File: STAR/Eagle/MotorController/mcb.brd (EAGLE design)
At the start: 28 x 35.5 mm, 38 parts, among them J1 J30J-9J30, U1 ATMEGA328P-MU, U2 A4988SETTR-T, U3 LT3010, U4 LT8630

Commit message: mcb update
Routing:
- net GND: track 192.5 -> 192.6 mm, vias 23 -> 25
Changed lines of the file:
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@@
 <setting verticaltext="up"/>
 </settings>
-<grid distance="0.1" unitdist="mm" unit="mm" style="lines" multiple="1" display="yes" altdistance="0.025" altunitdist="inch" altunit="inch"/>
+<grid distance="0.05" unitdist="mm" unit="mm" style="lines" multiple="1" display="yes" altdistance="0.025" altunitdist="inch" altunit="inch"/>
 <layers>
 <layer number="1" name="Top" color="4" fill="1" visible="yes" active="yes"/>
@@
 <wire x1="8.51" y1="10.2" x2="7.6" y2="10.2" width="0.3048" layer="1"/>
 <via x="7.6" y="10.2" extent="1-16" drill="0.5"/>
-<wire x1="7.6" y1="10.2" x2="6.1" y2="8.7" width="0.3048" layer="16"/>
-<via x="6.1" y="8.7" extent="1-16" drill="0.5"/>
-<wire x1="6.1" y1="8.7" x2="5.87" y2="8.47" width="0.3048" layer="1"/>
+<wire x1="7.6" y1="10.2" x2="6" y2="8.9" width="0.3048" layer="16"/>
+<via x="6" y="8.9" extent="1-16" drill="0.5"/>
+<wire x1="6" y1="8.9" x2="5.87" y2="8.47" width="0.3048" layer="1"/>
 <wire x1="5.87" y1="8.47" x2="5.19" y2="8.47" width="0.3048" layer="1"/>
 <wire x1="13.97" y1="17.41" x2="14.1" y2="17.54" width="0.254" layer="1"/>
@@
 <wire x1="22.7" y1="0.6" x2="22.7" y2="1.3" width="0.3048" layer="1"/>
 <via x="21.1" y="17.6" extent="1-16" drill="0.5"/>
+<via x="6.7" y="33.05" extent="1-16" drill="0.5"/>
+<via x="9.4" y="24.4" extent="1-16" drill="0.5"/>
 </signal>
 <signal name="+5V">
@@
 <wire x1="17.25" y1="17" x2="15.5" y2="17" width="0.3048" layer="16"/>
 <wire x1="15.5" y1="17" x2="14.5" y2="16" width="0.3048" layer="16"/>
-<wire x1="14.5" y1="16" x2="14.5" y2="15" width="0.3048" layer="16"/>
-<via x="14.5" y="15" extent="1-16" drill="0.5"/>
+<wire x1="14.5" y1="16" x2="14.5" y2="14.8" width="0.3048" layer="16"/>
+<via x="14.5" y="14.8" extent="1-16" drill="0.5"/>
 <wire x1="16.352" y1="12.3822" x2="16.352" y2="12.898" width="0.3048" layer="1"/>
 <wire x1="16.352" y1="12.898" x2="15.25" y2="14" width="0.3048" layer="1"/>
 <wire x1="15.25" y1="14" x2="15.25" y2="14.5" width="0.3048" layer="1"/>
-<wire x1="15.25" y1="14.5" x2="14.75" y2="15" width="0.3048" layer="1"/>
-<wire x1="14.75" y1="15" x2="14.5" y2="15" width="0.3048" layer="1"/>
+<wire x1="15.25" y1="14.5" x2="14.95" y2="14.8" width="0.3048" layer="1"/>
+<wire x1="14.95" y1="14.8" x2="14.5" y2="14.8" width="0.3048" layer="1"/>
 </signal>
 <signal name="STEP">
@@
 <wire x1="21.7794" y1="9.0294" x2="22.25" y2="9.5" width="0.3048" layer="1"/>
 <via x="22.25" y="9.5" extent="1-16" drill="0.5"/>
-<wire x1="22.25" y1="9.5" x2="22.25" y2="10.5" width="0.3048" layer="16"/>
-<wire x1="22.25" y1="10.5" x2="17" y2="15.75" width="0.3048" layer="16"/>
 <via x="17" y="15.75" extent="1-16" drill="0.5"/>
 <wire x1="17.948" y1="16.698" x2="18.6562" y2="16.698" width="0.3048" layer="1"/>
 <wire x1="17" y1="15.75" x2="17.948" y2="16.698" width="0.3048" layer="1"/>
+<wire x1="17" y1="15.75" x2="17" y2="15.65" width="0.3048" layer="16"/>
+<wire x1="17" y1="15.65" x2="19.2" y2="13.45" width="0.3048" layer="16"/>
+<wire x1="19.2" y1="13.45" x2="19.3" y2="13.35" width="0.3048" layer="16"/>
+<wire x1="22.25" y1="9.5" x2="22.25" y2="10.4" width="0.3048" layer="16"/>
+<wire x1="22.25" y1="10.4" x2="19.3" y2="13.35" width="0.3048" layer="16"/>
 </signal>
 <signal name="MS2">
@@
 <wire x1="20.238" y1="9.512" x2="20.15" y2="9.5" width="0.3048" layer="1"/>
 <via x="20.15" y="9.5" extent="1-16" drill="0.5"/>
-<via x="16.25" y="14.75" extent="1-16" drill="0.5"/>
+<via x="16.45" y="14.75" extent="1-16" drill="0.5"/>
 <wire x1="18.2154" y1="16.2154" x2="18.6562" y2="16.2154" width="0.3048" layer="1"/>
 <wire x1="20.25" y1="10.5" x2="17" y2="13.75" width="0.3048" layer="16"/>
 <wire x1="17" y1="13.75" x2="17" y2="14.25" width="0.3048" layer="16"/>
-<wire x1="17" y1="14.25" x2="16.5" y2="14.75" width="0.3048" layer="16"/>
-<wire x1="16.5" y1="14.75" x2="16.25" y2="14.75" width="0.3048" layer="16"/>
-<wire x1="16.25" y1="14.75" x2="17" y2="14.75" width="0.3048" layer="1"/>
 <wire x1="17" y1="14.75" x2="17.75" y2="15.5" width="0.3048" layer="1"/>
 <wire x1="18.2154" y1="16.2154" x2="17.75" y2="15.75" width="0.3048" layer="1"/>
@@
 <wire x1="19.2222" y1="9.512" x2="20.138" y2="9.512" width="0.3048" layer="1"/>
 <wire x1="20.138" y1="9.512" x2="20.15" y2="9.5" width="0.3048" layer="1"/>
+<wire x1="17" y1="14.25" x2="16.5" y2="14.75" width="0.3048" layer="16"/>
+<wire x1="16.5" y1="14.75" x2="16.45" y2="14.75" width="0.3048" layer="16"/>
+<wire x1="17" y1="14.75" x2="16.45" y2="14.75" width="0.3048" layer="1"/>
 </signal>
 <signal name="MS3">
@@
 <via x="21.25" y="10" extent="1-16" drill="0.5"/>
 <wire x1="21.25" y1="10" x2="21.25" y2="10.25" width="0.3048" layer="16"/>
-<wire x1="21.25" y1="10.25" x2="17.5" y2="14" width="0.3048" layer="16"/>
-<via x="17.5" y="14" extent="1-16" drill="0.5"/>
-<wire x1="17.5" y1="14" x2="17.5" y2="14.5512" width="0.3048" layer="1"/>
-<wire x1="17.5" y1="14.5512" x2="18.6562" y2="15.7074" width="0.3048" layer="1"/>
+<via x="17.7" y="14.1" extent="1-16" drill="0.5"/>
+<wire x1="21.25" y1="10.25" x2="17.7" y2="13.8" width="0.3048" layer="16"/>
+<wire x1="17.7" y1="13.8" x2="17.7" y2="14.1" width="0.3048" layer="16"/>
+<wire x1="17.7" y1="14.1" x2="17.7" y2="14.7512" width="0.3048" layer="1"/>
+<wire x1="17.7" y1="14.7512" x2="18.6562" y2="15.7074" width="0.3048" layer="1"/>
 </signal>
 <signal name="RESET~">

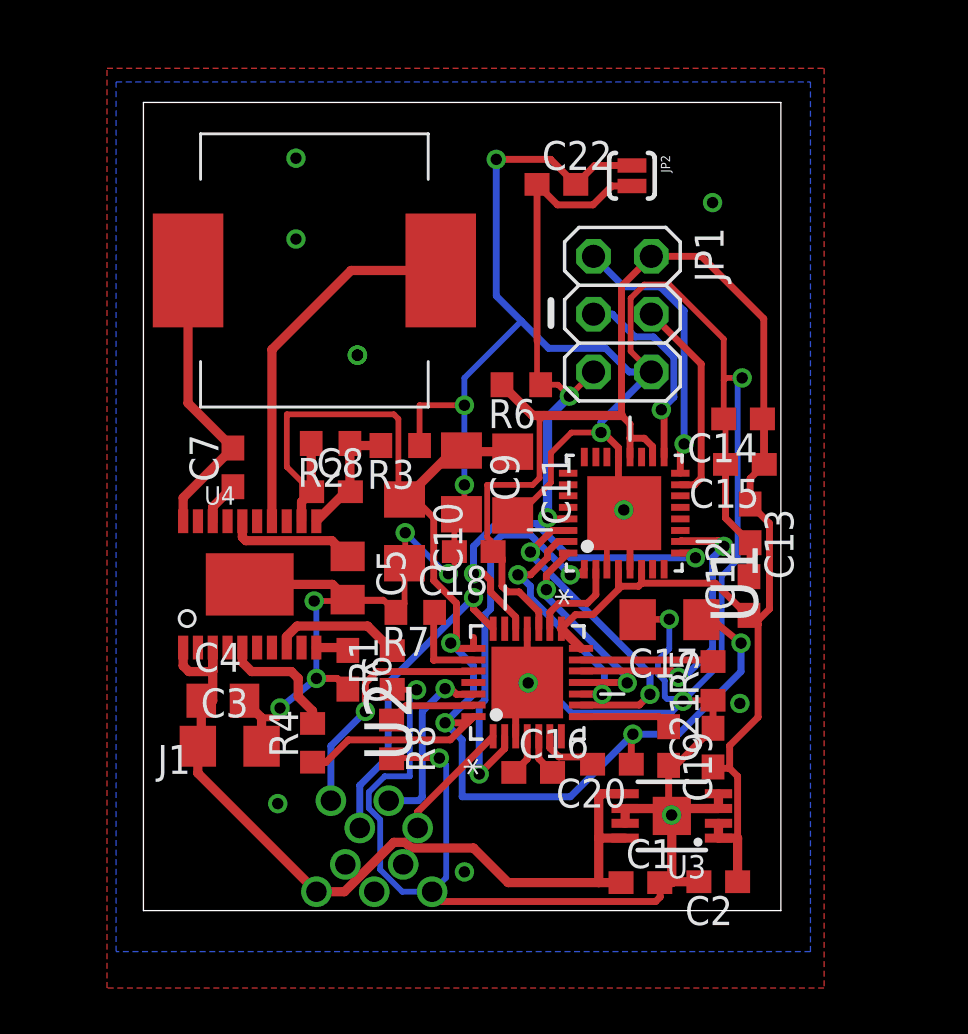
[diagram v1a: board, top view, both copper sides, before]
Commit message: increased room for C16
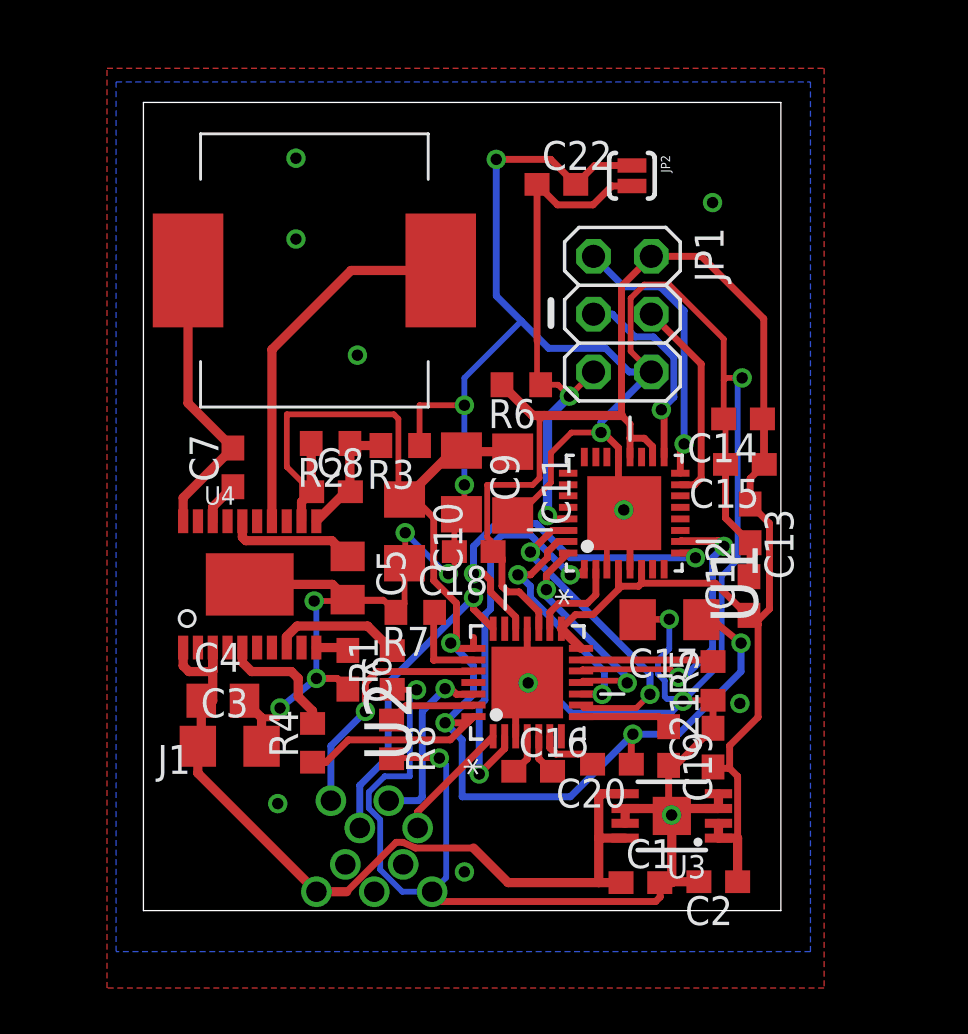
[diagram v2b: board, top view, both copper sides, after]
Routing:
- net GND: vias 25 -> 24
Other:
- board text added: "UMDBPP ROCKSAT-X 2018 MCB Rev 1.0"
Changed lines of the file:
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@@
 <setting verticaltext="up"/>
 </settings>
-<grid distance="0.05" unitdist="mm" unit="mm" style="lines" multiple="1" display="yes" altdistance="0.025" altunitdist="inch" altunit="inch"/>
+<grid distance="0.1" unitdist="mm" unit="mm" style="lines" multiple="1" display="yes" altdistance="0.025" altunitdist="inch" altunit="inch"/>
 <layers>
 <layer number="1" name="Top" color="4" fill="1" visible="yes" active="yes"/>
@@
 <layer number="20" name="Dimension" color="15" fill="1" visible="yes" active="yes"/>
 <layer number="21" name="tPlace" color="7" fill="1" visible="yes" active="yes"/>
-<layer number="22" name="bPlace" color="7" fill="1" visible="no" active="yes"/>
-<layer number="23" name="tOrigins" color="15" fill="1" visible="yes" active="yes"/>
+<layer number="22" name="bPlace" color="7" fill="1" visible="yes" active="yes"/>
+<layer number="23" name="tOrigins" color="15" fill="1" visible="no" active="yes"/>
 <layer number="24" name="bOrigins" color="15" fill="1" visible="no" active="yes"/>
 <layer number="25" name="tNames" color="7" fill="1" visible="no" active="yes"/>
@@
 <dimension x1="0" y1="0" x2="28" y2="0" x3="14" y3="-4.8" textsize="1.778" layer="51"/>
 <dimension x1="28" y1="35.5" x2="28" y2="0" x3="36.7" y3="17.75" textsize="1.778" layer="51"/>
+<text x="4.9" y="11.1" size="1.016" layer="22" rot="MR270">UMDBPP
+ROCKSAT-X 2018
+MCB Rev 1.0</text>
 </plain>
 <attributes>
@@
 <element name="C14" library="resistor" package="C0603" value="1uF" x="26.34" y="21.6" rot="R180"/>
 <element name="C15" library="resistor" package="C0603" value="1uF" x="26.42" y="19.6" rot="R180"/>
-<element name="C16" library="resistor" package="C0603" value="100nF" x="17.12" y="6.07"/>
+<element name="C16" library="resistor" package="C0603" value="100nF" x="17.12" y="6.12"/>
 <element name="C17" library="resistor" package="C1206" value="10uF" x="23.11" y="12.78" rot="R180"/>
 <element name="C18" library="resistor" package="C0603" value="1uF" x="14.51" y="15.77" rot="R180"/>
@@
 </polygon>
 <via x="6.7" y="29.5" extent="1-16" drill="0.5"/>
-<via x="9.4" y="24.4" extent="1-16" drill="0.5"/>
 <via x="25" y="31.1" extent="1-16" drill="0.5"/>
 <via x="26.2" y="9.1" extent="1-16" drill="0.5"/>
@@
 <wire x1="7.6" y1="0.83" x2="2.39" y2="6.04" width="0.4064" layer="1"/>
 <wire x1="2.39" y1="6.04" x2="2.39" y2="7.22" width="0.4064" layer="1"/>
-<wire x1="7.6" y1="0.83" x2="8.83" y2="0.83" width="0.4064" layer="1"/>
-<wire x1="8.83" y1="0.83" x2="11" y2="3" width="0.4064" layer="1"/>
-<wire x1="11" y1="3" x2="11.5" y2="3" width="0.4064" layer="1"/>
-<wire x1="11.5" y1="3" x2="11.75" y2="2.75" width="0.4064" layer="1"/>
-<wire x1="11.75" y1="2.75" x2="14.5" y2="2.75" width="0.4064" layer="1"/>
+<wire x1="7.6" y1="0.83" x2="8.93" y2="0.83" width="0.4064" layer="1"/>
+<wire x1="8.93" y1="0.83" x2="11.1" y2="3" width="0.3048" layer="1"/>
+<wire x1="11.1" y1="3" x2="11.4" y2="3" width="0.3048" layer="1"/>
+<wire x1="11.4" y1="3" x2="11.95" y2="2.75" width="0.3048" layer="1"/>
+<wire x1="11.95" y1="2.75" x2="14.5" y2="2.75" width="0.3048" layer="1"/>
 <wire x1="14.5" y1="2.75" x2="16.02" y2="1.23" width="0.4064" layer="1"/>
 <wire x1="16.02" y1="1.23" x2="20" y2="1.23" width="0.4064" layer="1"/>
@@
 <contactref element="U2" pad="5"/>
 <contactref element="C16" pad="2"/>
-<wire x1="17.97" y1="6.07" x2="17.368" y2="6.672" width="0.3048" layer="1"/>
+<wire x1="17.97" y1="6.12" x2="17.368" y2="6.672" width="0.3048" layer="1"/>
 <wire x1="17.368" y1="6.672" x2="17.368" y2="7.6578" width="0.3048" layer="1"/>
 </signal>
@@
 <contactref element="C16" pad="1"/>
 <contactref element="U2" pad="4"/>
-<wire x1="16.27" y1="6.07" x2="16.86" y2="6.66" width="0.3048" layer="1"/>
+<wire x1="16.27" y1="6.12" x2="16.86" y2="6.66" width="0.3048" layer="1"/>
 <wire x1="16.86" y1="6.66" x2="16.86" y2="7.6578" width="0.3048" layer="1"/>
 </signal>
@@
 <contactref element="C20" pad="2"/>
 <wire x1="17.8506" y1="7.6578" x2="17.8506" y2="7.1494" width="0.3048" layer="1"/>
-<wire x1="17.8506" y1="7.1494" x2="18.25" y2="6.75" width="0.3048" layer="1"/>
-<wire x1="18.25" y1="6.75" x2="19.41" y2="6.75" width="0.3048" layer="1"/>
-<wire x1="19.41" y1="6.75" x2="19.73" y2="6.43" width="0.3048" layer="1"/>
+<wire x1="17.8506" y1="7.1494" x2="18.125" y2="6.875" width="0.3048" layer="1"/>
+<wire x1="18.125" y1="6.875" x2="19.285" y2="6.875" width="0.3048" layer="1"/>
+<wire x1="19.285" y1="6.875" x2="19.73" y2="6.43" width="0.3048" layer="1"/>
 </signal>
 <signal name="ENABLE~">
@@
 <contactref element="U2" pad="9"/>
 <contactref element="U1" pad="30"/>
-<wire x1="19.2222" y1="9.0294" x2="21.7794" y2="9.0294" width="0.3048" layer="1"/>
-<wire x1="21.7794" y1="9.0294" x2="22.25" y2="9.5" width="0.3048" layer="1"/>
 <via x="22.25" y="9.5" extent="1-16" drill="0.5"/>
 <via x="17" y="15.75" extent="1-16" drill="0.5"/>
@@
 <wire x1="17" y1="15.75" x2="17.948" y2="16.698" width="0.3048" layer="1"/>
 <wire x1="17" y1="15.75" x2="17" y2="15.65" width="0.3048" layer="16"/>
-<wire x1="17" y1="15.65" x2="19.2" y2="13.45" width="0.3048" layer="16"/>
-<wire x1="19.2" y1="13.45" x2="19.3" y2="13.35" width="0.3048" layer="16"/>
 <wire x1="22.25" y1="9.5" x2="22.25" y2="10.4" width="0.3048" layer="16"/>
-<wire x1="22.25" y1="10.4" x2="19.3" y2="13.35" width="0.3048" layer="16"/>
+<wire x1="22.25" y1="10.4" x2="17" y2="15.65" width="0.3048" layer="16"/>
+<wire x1="19.2222" y1="9.0294" x2="19.3516" y2="8.9" width="0.254" layer="1"/>
+<wire x1="19.3516" y1="8.9" x2="21.65" y2="8.9" width="0.254" layer="1"/>
+<wire x1="21.65" y1="8.9" x2="22.25" y2="9.5" width="0.254" layer="1"/>
 </signal>
 <signal name="MS2">
@@
 <contactref element="U2" pad="11"/>
 <contactref element="U1" pad="32"/>
-<wire x1="19.2222" y1="10.02" x2="21.23" y2="10.02" width="0.3048" layer="1"/>
 <wire x1="21.23" y1="10.02" x2="21.25" y2="10" width="0.3048" layer="1"/>
 <via x="21.25" y="10" extent="1-16" drill="0.5"/>
@@
 <wire x1="17.7" y1="14.1" x2="17.7" y2="14.7512" width="0.3048" layer="1"/>
 <wire x1="17.7" y1="14.7512" x2="18.6562" y2="15.7074" width="0.3048" layer="1"/>
+<wire x1="19.2222" y1="10.02" x2="19.3022" y2="10.1" width="0.254" layer="1"/>
+<wire x1="19.3022" y1="10.1" x2="21.15" y2="10.1" width="0.254" layer="1"/>
+<wire x1="21.15" y1="10.1" x2="21.25" y2="10" width="0.254" layer="1"/>
 </signal>
 <signal name="RESET~">
 <contactref element="U2" pad="12"/>
 <contactref element="U1" pad="10"/>
-<wire x1="19.2222" y1="10.528" x2="23.222" y2="10.528" width="0.3048" layer="1"/>
-<wire x1="23.222" y1="10.528" x2="23.5" y2="10.25" width="0.3048" layer="1"/>
 <via x="23.5" y="10.25" extent="1-16" drill="0.5"/>
 <wire x1="25.5" y1="16" x2="25.2846" y2="16.2154" width="0.3048" layer="1"/>
@@
 <wire x1="25" y1="11.5" x2="23.75" y2="10.25" width="0.3048" layer="16"/>
 <wire x1="23.75" y1="10.25" x2="23.5" y2="10.25" width="0.3048" layer="16"/>
+<wire x1="19.2222" y1="10.528" x2="19.2942" y2="10.6" width="0.254" layer="1"/>
+<wire x1="19.2942" y1="10.6" x2="23.15" y2="10.6" width="0.254" layer="1"/>
+<wire x1="23.15" y1="10.6" x2="23.5" y2="10.25" width="0.254" layer="1"/>
 </signal>
 <signal name="MOSI">
@@
 <via x="18.71" y="22.6" extent="1-16" drill="0.5"/>
 <wire x1="18.71" y1="22.6" x2="17.75" y2="21.64" width="0.4064" layer="16"/>
-<wire x1="17.75" y1="21.64" x2="17.75" y2="17.25" width="0.4064" layer="16"/>
-<via x="17.75" y="17.25" extent="1-16" drill="0.5"/>
-<wire x1="17.75" y1="17.25" x2="17.794" y2="17.206" width="0.3048" layer="1"/>
-<wire x1="17.794" y1="17.206" x2="18.6562" y2="17.206" width="0.3048" layer="1"/>
+<wire x1="17.75" y1="21.64" x2="17.75" y2="17.35" width="0.4064" layer="16"/>
+<via x="17.75" y="17.35" extent="1-16" drill="0.5"/>
+<wire x1="17.75" y1="17.35" x2="17.894" y2="17.206" width="0.3048" layer="1"/>
+<wire x1="17.894" y1="17.206" x2="18.6562" y2="17.206" width="0.3048" layer="1"/>
 <wire x1="18.71" y1="22.6" x2="19.77" y2="23.66" width="0.254" layer="1"/>
 <wire x1="18.71" y1="22.6" x2="18.21" y2="23.1" width="0.254" layer="1"/>
@@
 </board>
 </drawing>
+<compatibility>
+<note version="6.3" minversion="6.2.2" severity="warning">
+Since Version 6.2.2 text objects can contain more than one line,
+which will not be processed correctly with this version.
+</note>
+</compatibility>
 </eagle>

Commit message: mounting holes on mcb
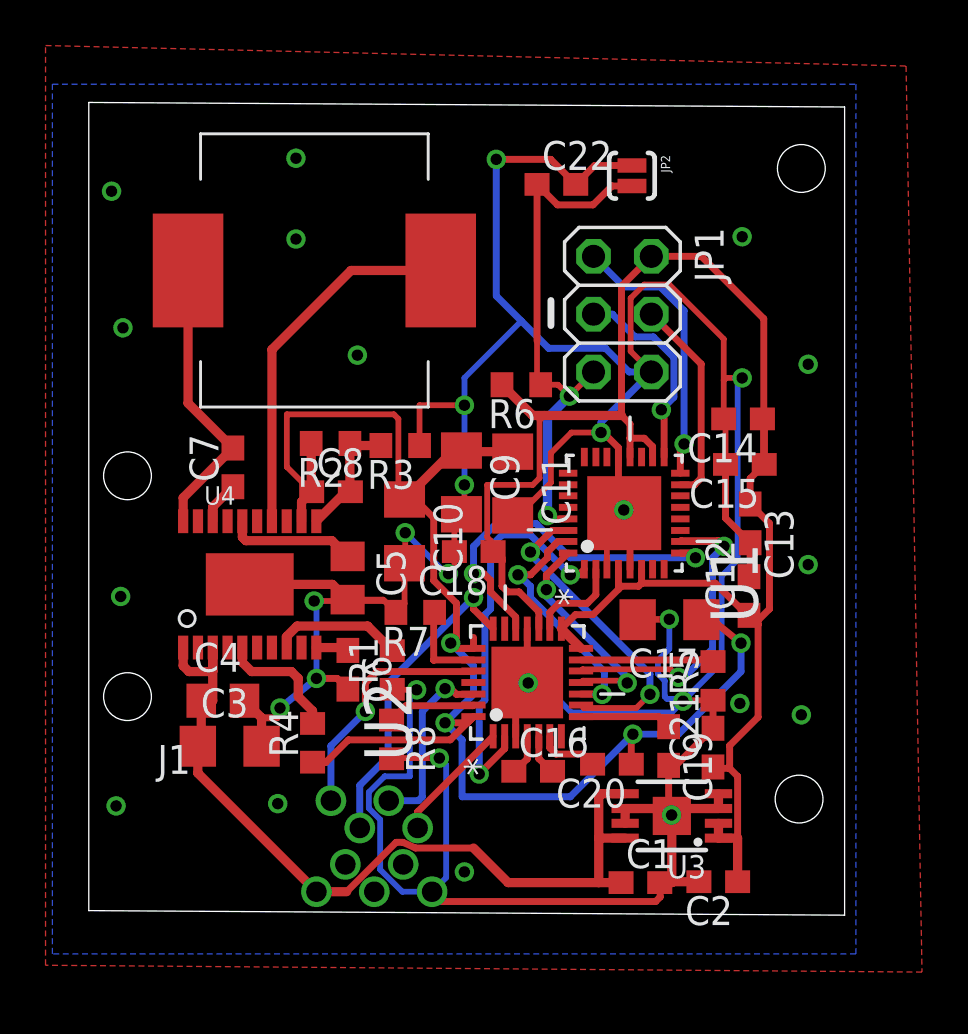
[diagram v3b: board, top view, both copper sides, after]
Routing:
- net GND: vias 24 -> 31
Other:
- board size 28 x 35.5 mm -> 33.2 x 35.7 mm
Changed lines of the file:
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@@
 <layer number="43" name="vRestrict" color="2" fill="10" visible="no" active="yes"/>
 <layer number="44" name="Drills" color="7" fill="1" visible="no" active="yes"/>
-<layer number="45" name="Holes" color="7" fill="1" visible="no" active="yes"/>
+<layer number="45" name="Holes" color="7" fill="1" visible="yes" active="yes"/>
 <layer number="46" name="Milling" color="3" fill="1" visible="no" active="yes"/>
 <layer number="47" name="Measures" color="7" fill="1" visible="no" active="yes"/>
@@
 <board>
 <plain>
-<wire x1="0" y1="0" x2="28" y2="0" width="0" layer="20"/>
-<wire x1="28" y1="0" x2="28" y2="35.5" width="0" layer="20"/>
-<wire x1="28" y1="35.5" x2="0" y2="35.5" width="0" layer="20"/>
-<wire x1="0" y1="35.5" x2="0" y2="0" width="0" layer="20"/>
+<wire x1="-2.4" y1="0" x2="30.8" y2="-0.2" width="0" layer="20"/>
+<wire x1="30.8" y1="-0.2" x2="30.8" y2="35.3" width="0" layer="20"/>
+<wire x1="30.8" y1="35.3" x2="-2.4" y2="35.5" width="0" layer="20"/>
+<wire x1="-2.4" y1="35.5" x2="-2.4" y2="0" width="0" layer="20"/>
 <wire x1="17.9" y1="26.8" x2="17.9" y2="25.7" width="0.3048" layer="21"/>
 <circle x="15.5" y="8.6" radius="0.14141875" width="0.3048" layer="21"/>
@@
 ROCKSAT-X 2018
 MCB Rev 1.0</text>
+<hole x="28.9" y="32.6" drill="2.1"/>
+<hole x="28.8" y="4.9" drill="2.1"/>
+<hole x="-0.7" y="9.4" drill="2.1"/>
+<hole x="-0.7" y="19.1" drill="2.1"/>
 </plain>
 <attributes>
@@
 <wire x1="10.4" y1="1.8" x2="10.4" y2="4" width="0.254" layer="16"/>
 <polygon width="0.3048" layer="1">
-<vertex x="-1.6" y="37"/>
-<vertex x="29.9" y="37"/>
-<vertex x="29.9" y="-3.4"/>
-<vertex x="-1.6" y="-3.4"/>
+<vertex x="-4.3" y="38"/>
+<vertex x="33.5" y="37.1"/>
+<vertex x="34.2" y="-2.7"/>
+<vertex x="-4.3" y="-2.4"/>
 </polygon>
 <polygon width="0.3048" layer="16">
-<vertex x="-1.2" y="36.4"/>
-<vertex x="29.3" y="36.4"/>
-<vertex x="29.3" y="-1.8"/>
-<vertex x="-1.2" y="-1.8"/>
+<vertex x="-4" y="36.3"/>
+<vertex x="31.3" y="36.3"/>
+<vertex x="31.3" y="-1.9"/>
+<vertex x="-4" y="-1.9"/>
 </polygon>
 <via x="6.7" y="29.5" extent="1-16" drill="0.5"/>
-<via x="25" y="31.1" extent="1-16" drill="0.5"/>
+<via x="26.3" y="29.6" extent="1-16" drill="0.5"/>
 <via x="26.2" y="9.1" extent="1-16" drill="0.5"/>
 <via x="14.1" y="1.7" extent="1-16" drill="0.5"/>
@@
 <via x="6.7" y="33.05" extent="1-16" drill="0.5"/>
 <via x="9.4" y="24.4" extent="1-16" drill="0.5"/>
+<via x="29.2" y="24" extent="1-16" drill="0.5"/>
+<via x="29.2" y="15.2" extent="1-16" drill="0.5"/>
+<via x="28.9" y="8.6" extent="1-16" drill="0.5"/>
+<via x="-1" y="13.8" extent="1-16" drill="0.5"/>
+<via x="-1.2" y="4.6" extent="1-16" drill="0.5"/>
+<via x="-0.9" y="25.6" extent="1-16" drill="0.5"/>
+<via x="-1.4" y="31.6" extent="1-16" drill="0.5"/>
 </signal>
 <signal name="+5V">
